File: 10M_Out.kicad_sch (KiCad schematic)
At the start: 10 parts, among them U4 74HC04

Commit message: Fix footprint of C19 JLCPCB DFM identified 0805 part fitted on 1206 footprint
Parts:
- C19: footprint Capacitor_SMD:C_1206_3216Metric_Pad1.33x1.80mm_HandSolder -> Capacitor_SMD:C_0805_2012Metric_Pad1.18x1.45mm_HandSolder
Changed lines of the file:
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@@
       (effects (font (size 1.27 1.27)) (justify left))
     )
-    (property "Footprint" "Capacitor_SMD:C_1206_3216Metric_Pad1.33x1.80mm_HandSolder" (id 2) (at 124.1552 46.99 0)
+    (property "Footprint" "Capacitor_SMD:C_0805_2012Metric_Pad1.18x1.45mm_HandSolder" (id 2) (at 124.1552 46.99 0)
       (effects (font (size 1.27 1.27)) hide)
     )

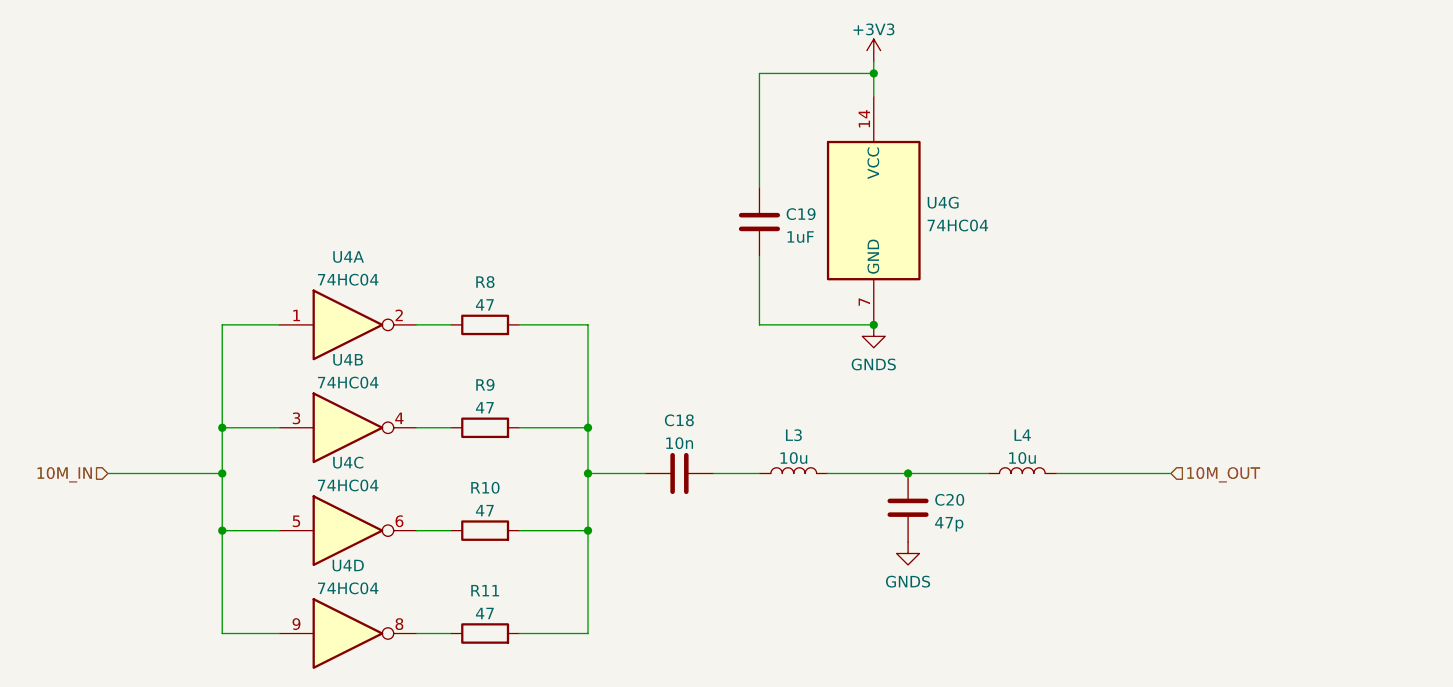
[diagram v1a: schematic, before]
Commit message: Fix 10M output filter
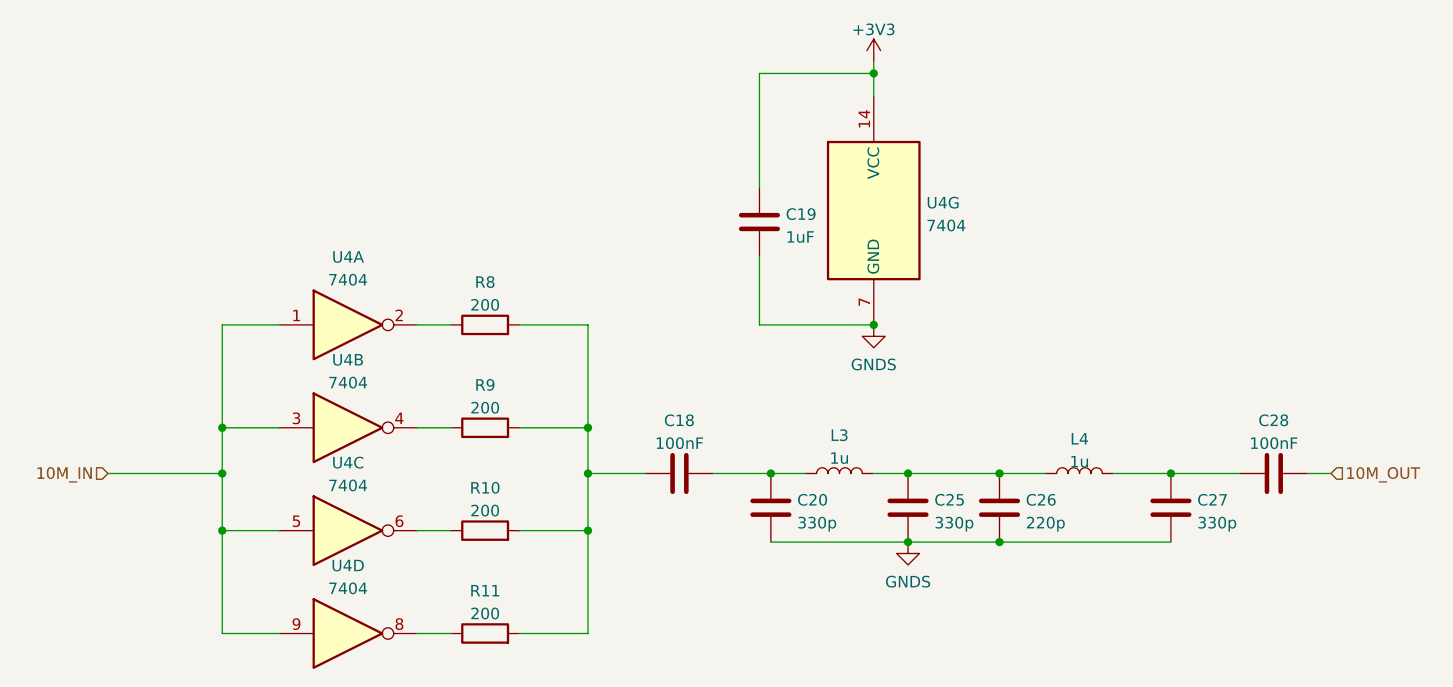
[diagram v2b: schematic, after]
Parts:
- added C25, C27: 330p, Capacitor_SMD:C_0603_1608Metric_Pad1.08x0.95mm_HandSolder, symbol Device:C
- added C26: 220p, Capacitor_SMD:C_0603_1608Metric_Pad1.08x0.95mm_HandSolder, symbol Device:C
- added C28: 100nF, Capacitor_SMD:C_0805_2012Metric_Pad1.18x1.45mm_HandSolder, symbol Device:C
- C18: value 10n -> 100nF; LCSC C1710 -> C49678
- C20: value 47p -> 330p; footprint Capacitor_SMD:C_0805_2012Metric_Pad1.18x1.45mm_HandSolder -> Capacitor_SMD:C_0603_1608Metric_Pad1.08x0.95mm_HandSolder; LCSC C14857 -> C1664
- L3, L4: value 10u -> 1u; footprint Inductor_SMD:L_1206_3216Metric_Pad1.22x1.90mm_HandSolder -> Inductor_SMD:L_0805_2012Metric_Pad1.15x1.40mm_HandSolder; LCSC C1051 -> C1042
- R10, R11, R8, R9: value 47 -> 200; LCSC C17714 -> C17540
- U4: value 74HC04 -> 7404
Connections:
- net 10M_OUT: now also C28.1; no longer L4.2
- net GNDS: now also C25.2, C26.2, C27.2
- net at R10.2, R11.2, R8.2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: now also C18.2; no longer C18.1
- net at L3.1: now also C18.1, C20.1; no longer C18.2
- net at L3.2, L4.1: now also C25.1, C26.1; no longer C20.1
- new net: C27.1, C28.2, L4.2
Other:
- moved on the sheet: L3, L4
